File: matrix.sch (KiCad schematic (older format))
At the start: 153 parts

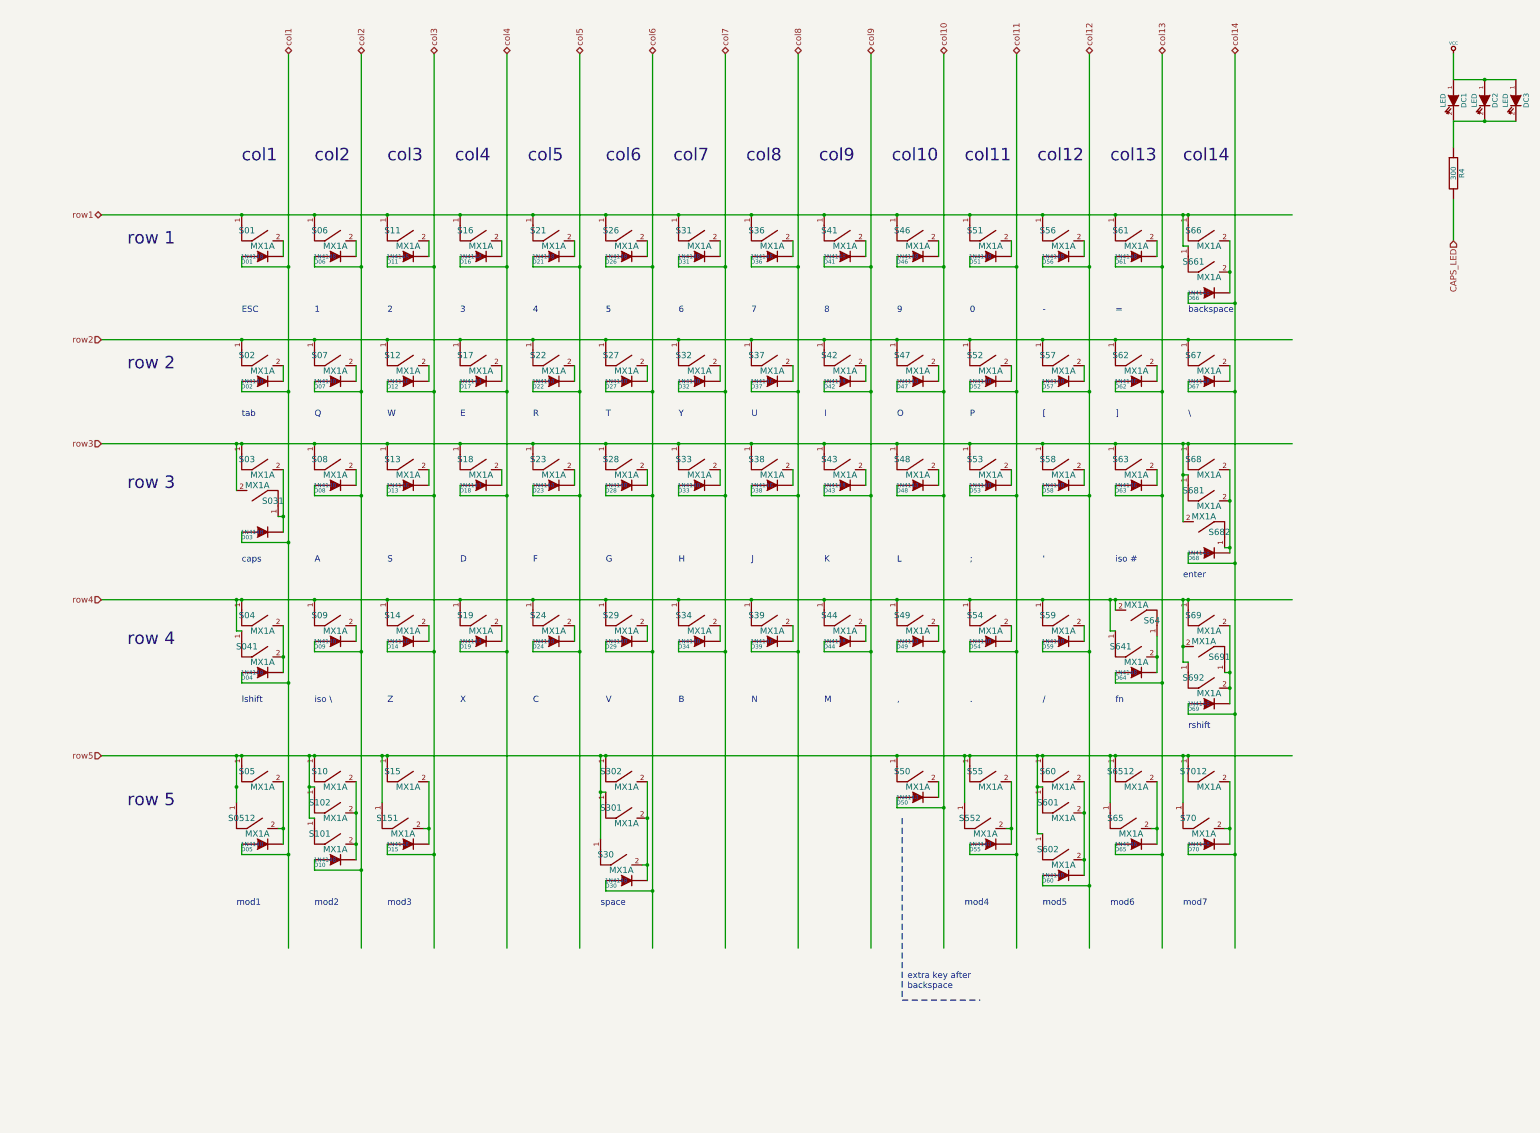
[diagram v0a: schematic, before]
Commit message: 修改usb接口为type c
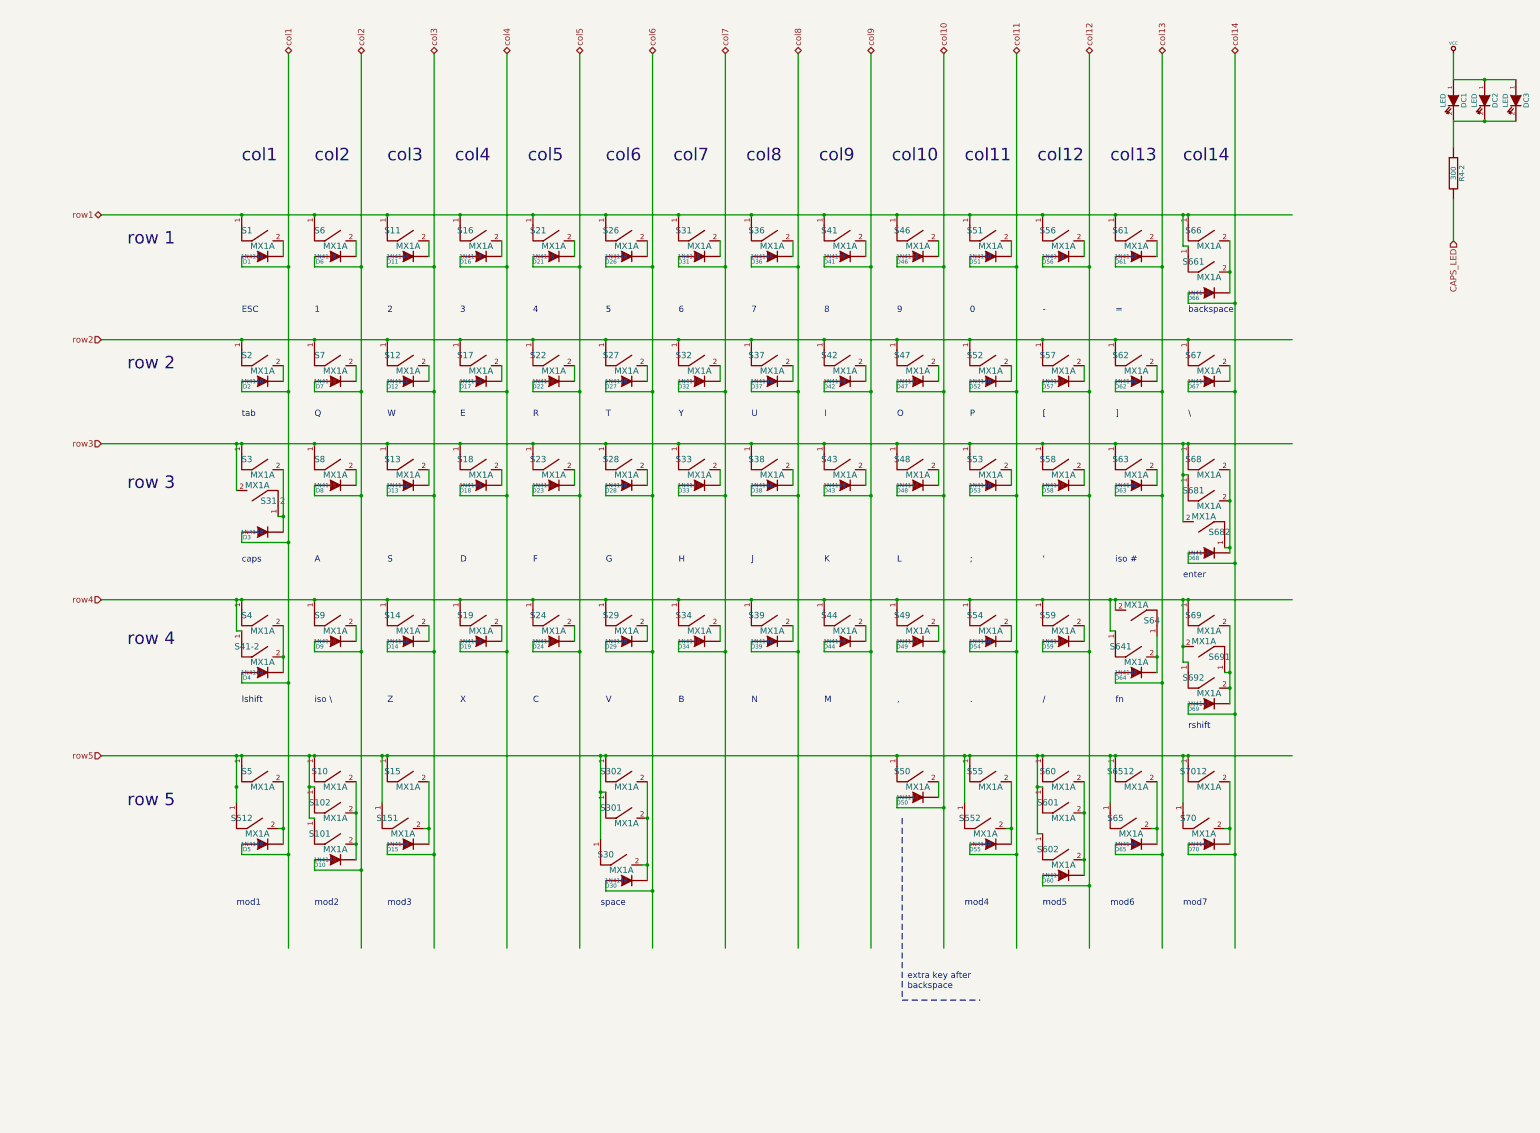
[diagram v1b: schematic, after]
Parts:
- renumbered D01 to D1, D02 to D2, D03 to D3, D04 to D4, D05 to D5, D06 to D6, D07 to D7, D08 to D8, D09 to D9, R4 to R4-2, S01 to S1, S02 to S2, S03 to S3, S031 to S31-2, S04 to S4, S041 to S41-2, S05 to S5, S0512 to S512, S06 to S6, S07 to S7, S08 to S8, S09 to S9
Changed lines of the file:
@@
 LIBS:device
 LIBS:conn
+LIBS:usb-type-c
 LIBS:keyboard-cache
 EELAYER 25 0
@@
 $Descr A3 16535 11693
 encoding utf-8
-Sheet 2 3
+Sheet 2 4
 Title ""
 Date "17 jul 2013"
@@
 $EndDescr
 $Comp
-L MX1A S01
+L MX1A S1
 U 1 1 5040DD75
 P 3350 3350
-F 0 "S01" H 3200 3600 60  0000 C CNN
+F 0 "S1" H 3200 3600 60  0000 C CNN
 F 1 "MX1A" H 3350 3450 60  0000 C CNN
 F 2 "mx1a:MX1A" H 3350 3350 60  0001 C CNN
@@
 $EndComp
 $Comp
-L MX1A S06
+L MX1A S6
 U 1 1 5040DD84
 P 4050 3350
-F 0 "S06" H 3900 3600 60  0000 C CNN
+F 0 "S6" H 3900 3600 60  0000 C CNN
 F 1 "MX1A" H 4050 3450 60  0000 C CNN
 F 2 "mx1a:MX1A" H 4050 3350 60  0001 C CNN
@@
 $EndComp
 $Comp
-L MX1A S02
+L MX1A S2
 U 1 1 5040DDF7
 P 3350 4550
-F 0 "S02" H 3200 4800 60  0000 C CNN
+F 0 "S2" H 3200 4800 60  0000 C CNN
 F 1 "MX1A" H 3350 4650 60  0000 C CNN
 F 2 "mx1a:MX1A" H 3350 4550 60  0001 C CNN
@@
 $EndComp
 $Comp
-L MX1A S07
+L MX1A S7
 U 1 1 5040DDFD
 P 4050 4550
-F 0 "S07" H 3900 4800 60  0000 C CNN
+F 0 "S7" H 3900 4800 60  0000 C CNN
 F 1 "MX1A" H 4050 4650 60  0000 C CNN
 F 2 "mx1a:MX1A" H 4050 4550 60  0001 C CNN
@@
 $EndComp
 $Comp
-L MX1A S03
+L MX1A S3
 U 1 1 5040DE57
 P 3350 5550
-F 0 "S03" H 3200 5800 60  0000 C CNN
+F 0 "S3" H 3200 5800 60  0000 C CNN
 F 1 "MX1A" H 3350 5650 60  0000 C CNN
 F 2 "mx1a:MX1A" H 3350 5550 60  0001 C CNN
@@
 $EndComp
 $Comp
-L MX1A S08
+L MX1A S8
 U 1 1 5040DE5D
 P 4050 5550
-F 0 "S08" H 3900 5800 60  0000 C CNN
+F 0 "S8" H 3900 5800 60  0000 C CNN
 F 1 "MX1A" H 4050 5650 60  0000 C CNN
 F 2 "mx1a:MX1A" H 4050 5550 60  0001 C CNN
@@
 $EndComp
 $Comp
-L MX1A S09
+L MX1A S9
 U 1 1 5040DEBD
 P 4050 7050
-F 0 "S09" H 3900 7300 60  0000 C CNN
+F 0 "S9" H 3900 7300 60  0000 C CNN
 F 1 "MX1A" H 4050 7150 60  0000 C CNN
 F 2 "mx1a:MX1A_no3d" H 4050 7050 60  0001 C CNN
@@
 $EndComp
 $Comp
-L MX1A S05
+L MX1A S5
 U 1 1 5040DF17
 P 3350 8550
-F 0 "S05" H 3200 8800 60  0000 C CNN
+F 0 "S5" H 3200 8800 60  0000 C CNN
 F 1 "MX1A" H 3350 8650 60  0000 C CNN
 F 2 "mx1a:MX1A" H 3350 8550 60  0001 C CNN
@@
 $EndComp
 $Comp
-L MX1A S0512
+L MX1A S512
 U 1 1 5040ECF7
 P 3300 9000
-F 0 "S0512" H 3150 9250 60  0000 C CNN
+F 0 "S512" H 3150 9250 60  0000 C CNN
 F 1 "MX1A" H 3300 9100 60  0000 C CNN
 F 2 "mx1a:MX1A_no3d" H 3300 9000 60  0001 C CNN
@@
 $EndComp
 $Comp
-L MX1A S041
+L MX1A S41-2
 U 1 1 50410564
 P 3350 7350
-F 0 "S041" H 3200 7600 60  0000 C CNN
+F 0 "S41-2" H 3200 7600 60  0000 C CNN
 F 1 "MX1A" H 3350 7450 60  0000 C CNN
 F 2 "mx1a:MX1A_no3d" H 3350 7350 60  0001 C CNN
@@
 $EndComp
 $Comp
-L MX1A S04
+L MX1A S4
 U 1 1 5040DEB7
 P 3350 7050
-F 0 "S04" H 3200 7300 60  0000 C CNN
+F 0 "S4" H 3200 7300 60  0000 C CNN
 F 1 "MX1A" H 3350 7150 60  0000 C CNN
 F 2 "mx1a:MX1A" H 3350 7050 60  0001 C CNN
@@
 col8
 $Comp
-L MX1A S031
+L MX1A S31-2
 U 1 1 5042A9E4
 P 3300 5450
-F 0 "S031" H 3150 5700 60  0000 C CNN
+F 0 "S31-2" H 3150 5700 60  0000 C CNN
 F 1 "MX1A" H 3300 5550 60  0000 C CNN
 F 2 "mx1a:MX1A_no3d" H 3300 5450 60  0001 C CNN
@@
 col14
 $Comp
-L VCC #PWR031
+L VCC #PWR029
 U 1 1 5043970C
 P 14800 1400
-F 0 "#PWR031" H 14800 1500 30  0001 C CNN
+F 0 "#PWR029" H 14800 1500 30  0001 C CNN
 F 1 "VCC" H 14800 1500 30  0000 C CNN
 F 2 "" H 14800 1400 60  0001 C CNN
@@
 $EndComp
 $Comp
-L R R4
+L R R4-2
 U 1 1 5043A0D0
 P 14800 2550
-F 0 "R4" V 14880 2550 50  0000 C CNN
+F 0 "R4-2" V 14880 2550 50  0000 C CNN
 F 1 "300" V 14800 2550 50  0000 C CNN
 F 2 "" H 14800 2550 60  0001 C CNN
@@
 $EndComp
 $Comp
-L DIODE D06
+L DIODE D6
 U 1 1 506B1C22
 P 4050 3350
-F 0 "D06" H 3900 3300 40  0000 C CNN
+F 0 "D6" H 3900 3300 40  0000 C CNN
 F 1 "1N4148" H 3950 3350 40  0000 C CNN
 F 2 "0805:0805D" H 4050 3350 60  0001 C CNN
@@
 $EndComp
 $Comp
-L DIODE D02
+L DIODE D2
 U 1 1 506B1C34
 P 3350 4550
-F 0 "D02" H 3200 4500 40  0000 C CNN
+F 0 "D2" H 3200 4500 40  0000 C CNN
 F 1 "1N4148" H 3250 4550 40  0000 C CNN
 F 2 "0805:0805D" H 3350 4550 60  0001 C CNN
@@
 $EndComp
 $Comp
-L DIODE D04
+L DIODE D4
 U 1 1 506B1C3D
 P 3350 7350
-F 0 "D04" H 3200 7300 40  0000 C CNN
+F 0 "D4" H 3200 7300 40  0000 C CNN
 F 1 "1N4148" H 3250 7350 40  0000 C CNN
 F 2 "0805:0805D" H 3350 7350 60  0001 C CNN
@@
 $EndComp
 $Comp
-L DIODE D07
+L DIODE D7
 U 1 1 506B1C46
 P 4050 4550
-F 0 "D07" H 3900 4500 40  0000 C CNN
+F 0 "D7" H 3900 4500 40  0000 C CNN
 F 1 "1N4148" H 3950 4550 40  0000 C CNN
 F 2 "0805:0805D" H 4050 4550 60  0001 C CNN
@@
 $EndComp
 $Comp
-L DIODE D08
+L DIODE D8
 U 1 1 506B1C4F
 P 4050 5550
-F 0 "D08" H 3900 5500 40  0000 C CNN
+F 0 "D8" H 3900 5500 40  0000 C CNN
 F 1 "1N4148" H 3950 5550 40  0000 C CNN
 F 2 "0805:0805D" H 4050 5550 60  0001 C CNN
@@
 $EndComp
 $Comp
-L DIODE D09
+L DIODE D9
 U 1 1 506B428A
 P 4050 7050
-F 0 "D09" H 3900 7000 40  0000 C CNN
+F 0 "D9" H 3900 7000 40  0000 C CNN
 F 1 "1N4148" H 3950 7050 40  0000 C CNN
 F 2 "0805:0805D" H 4050 7050 60  0001 C CNN
@@
 $EndComp
 $Comp
-L DIODE D01
+L DIODE D1
 U 1 1 506B5923
 P 3350 3350
-F 0 "D01" H 3200 3300 40  0000 C CNN
+F 0 "D1" H 3200 3300 40  0000 C CNN
 F 1 "1N4148" H 3250 3350 40  0000 C CNN
 F 2 "0805:0805D" H 3350 3350 60  0001 C CNN
@@
 $EndComp
 $Comp
-L DIODE D05
+L DIODE D5
 U 1 1 506B5A8B
 P 3350 9000
-F 0 "D05" H 3200 8950 40  0000 C CNN
+F 0 "D5" H 3200 8950 40  0000 C CNN
 F 1 "1N4148" H 3250 9000 40  0000 C CNN
 F 2 "0805:0805D" H 3350 9000 60  0001 C CNN
@@
 $EndComp
 $Comp
-L DIODE D03
+L DIODE D3
 U 1 1 506B5DE9
 P 3350 6000
-F 0 "D03" H 3200 5950 40  0000 C CNN
+F 0 "D3" H 3200 5950 40  0000 C CNN
 F 1 "1N4148" H 3250 6000 40  0000 C CNN
 F 2 "0805:0805D" H 3350 6000 60  0001 C CNN

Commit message: 增加一列F功能区 增加TrackPiont模块,同时增加ffc排线接口 右移右侧键布局
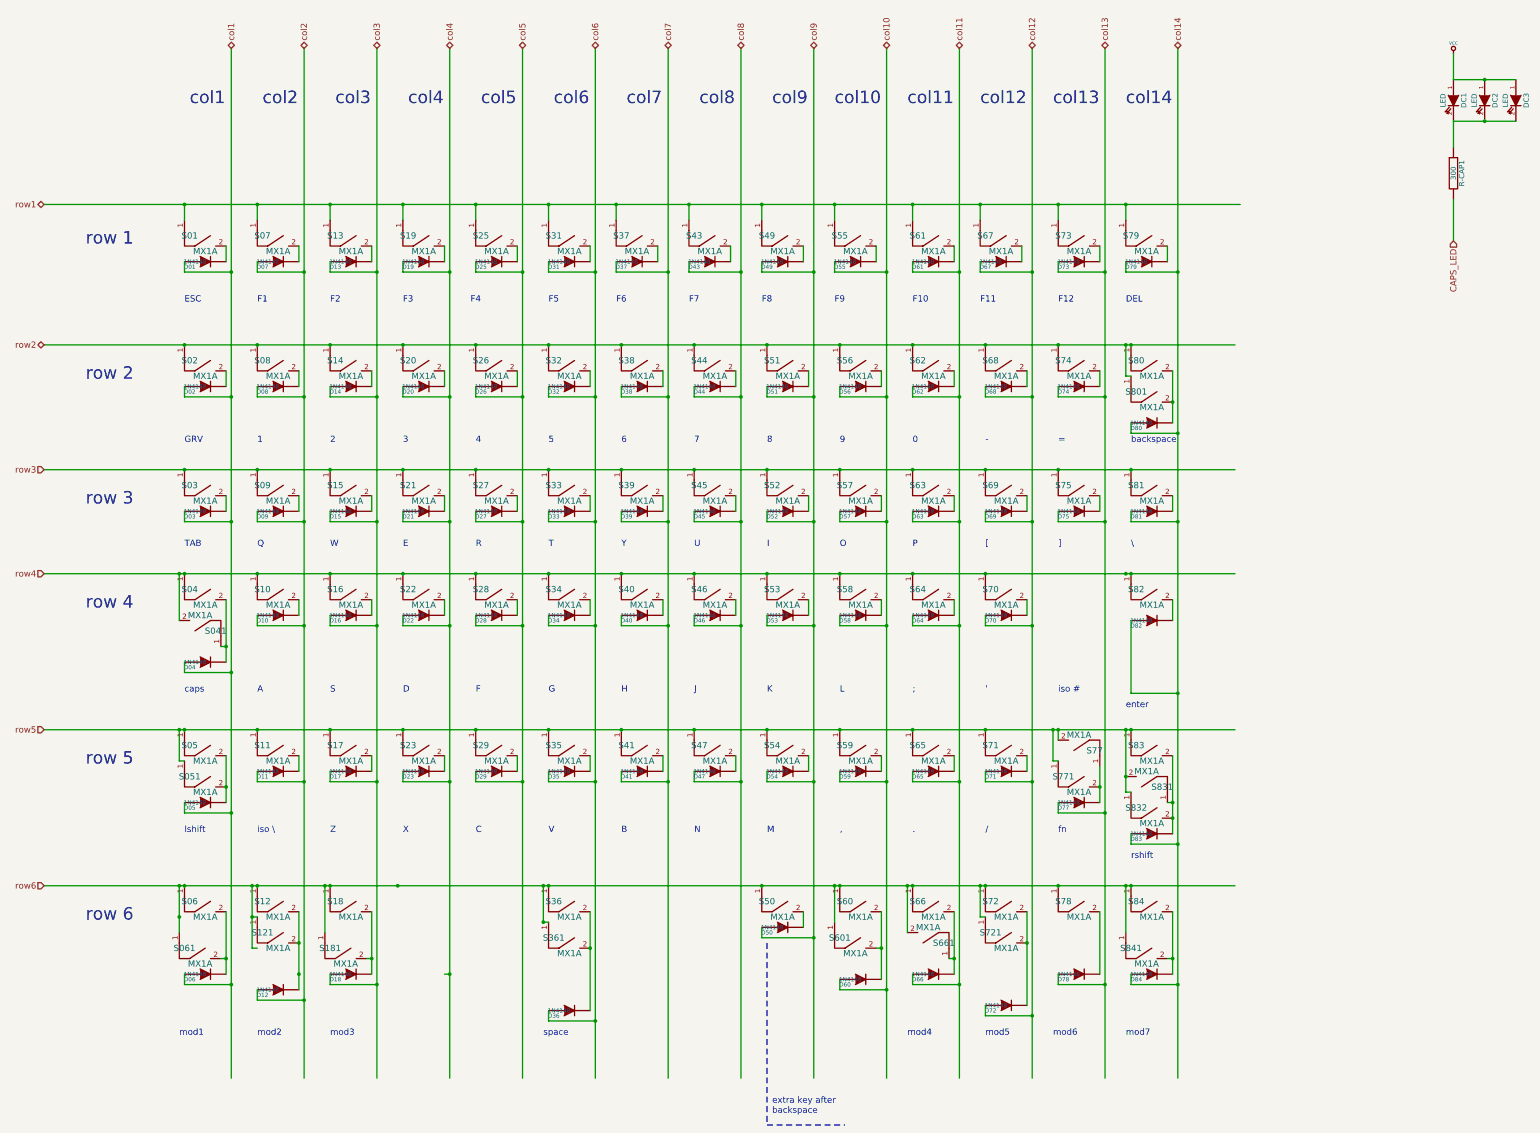
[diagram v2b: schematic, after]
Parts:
- removed D63: 1N4148, 0805:0805D, symbol DIODE
- removed S101, S602, S63, S681, S682: MX1A, mx1a:MX1A_no3d, symbol MX1A
- removed S30, S65: MX1A, mx1a:MX1A, symbol MX1A
- added D01, D07, D13, D19, D25, D31, D37, D43, D49, D50, D55, D61, D67, D73, D79: 1N4148, 0805:0805D, symbol DIODE
- added S01, S07, S13, S19, S25, S31, S37, S43, S49, S55, S601, S61, S67, S73, S79: MX1A, mx1a:MX1A, symbol MX1A
- added S50: MX1A, mx1a:MX1A_no3d, symbol MX1A
- R-CAP1: renamed from R4-2; footprint (none) -> 0805:0805R
- renumbered D1 to D02, D2 to D03, D3 to D04, D4 to D05, D5 to D06, D6 to D08, D7 to D09, D8 to D10, D9 to D11, D10 to D12, D11 to D14, D12 to D15, D13 to D16, D14 to D17, D15 to D18, D16 to D20, D17 to D21, D18 to D22, D19 to D23, D21 to D26, D22 to D27, D23 to D28, D24 to D29, D26 to D32, D27 to D33, D28 to D34, D29 to D35, D30 to D36, D31 to D38, D32 to D39, D33 to D40, D34 to D41, D36 to D44, D37 to D45, D38 to D46, D39 to D47, D41 to D51, D42 to D52, D43 to D53, D44 to D54, D46 to D56, D47 to D57, D48 to D58, D49 to D59, D50 to D60, D51 to D62, D52 to D63, D53 to D64, D54 to D65, D55 to D66, D56 to D68, D57 to D69, D58 to D70, D59 to D71, D60 to D72, D61 to D74, D62 to D75, D64 to D77, D65 to D78, D66 to D80, D67 to D81, D68 to D82, D69 to D83, D70 to D84, S1 to S02, S2 to S03, S3 to S04, S31-2 to S041, S4 to S05, S41-2 to S051, S5 to S06, S512 to S061, S6 to S08, S7 to S09, S8 to S10, S9 to S11, S10 to S12, S102 to S121, S11 to S14, S12 to S15, S13 to S16, S14 to S17, S15 to S18, S151 to S181, S16 to S20, S17 to S21, S18 to S22, S19 to S23, S21 to S26, S22 to S27, S23 to S28, S24 to S29, S26 to S32, S27 to S33, S28 to S34, S29 to S35, S302 to S36, S301 to S361, S31 to S38, S32 to S39, S33 to S40, S34 to S41, S36 to S44, S37 to S45, S38 to S46, S39 to S47, S41 to S51, S42 to S52, S43 to S53, S44 to S54, S46 to S56, S47 to S57, S48 to S58, S49 to S59, S50 to S60, S51 to S62, S52 to S63, S53 to S64, S54 to S65, S55 to S66, S552 to S661, S56 to S68, S57 to S69, S58 to S70, S59 to S71, S60 to S72, S601 to S721, S61 to S74, S62 to S75, S64 to S77, S641 to S771, S6512 to S78, S66 to S80, S661 to S801, S67 to S81, S68 to S82, S69 to S83, S691 to S831, S692 to S832, S7012 to S84, S70 to S841
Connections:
- net labels added: row6
- wire segments 254 -> 306
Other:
- note added: "DEL"
- note added: "F1"
- note added: "F10"
- note added: "F11"
- note added: "F12"
- note added: "F2"
- note added: "F3"
- note added: "F4"
- note added: "F5"
- note added: "F6"
- note added: "F7"
- note added: "F8"
- note added: "F9"
- note added: "GRV"
- note added: "TAB"
- note added: "row 6"
- note removed: "tab"
- moved on the sheet: D02, D03, D04, D05, D06, D08, D09, D10, D11, D12, D14, D15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
